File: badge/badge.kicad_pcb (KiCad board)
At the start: 2 copper layers, 39.4 x 73 mm, 13 parts, among them K1 KEYSW, K2 KEYSW, K3 KEYSW, K4 KEYSW, U1 ProMicro

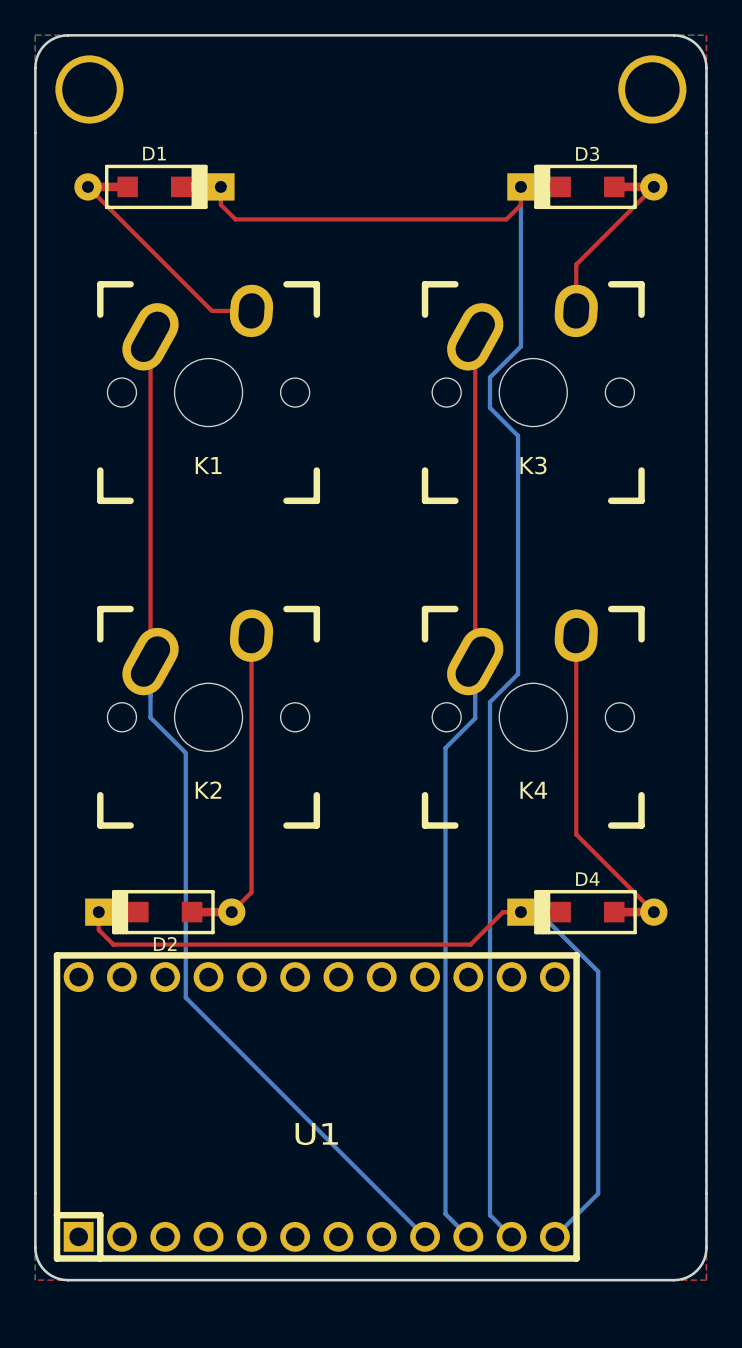
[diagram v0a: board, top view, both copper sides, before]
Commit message: Use different pro micro pins for easier routing
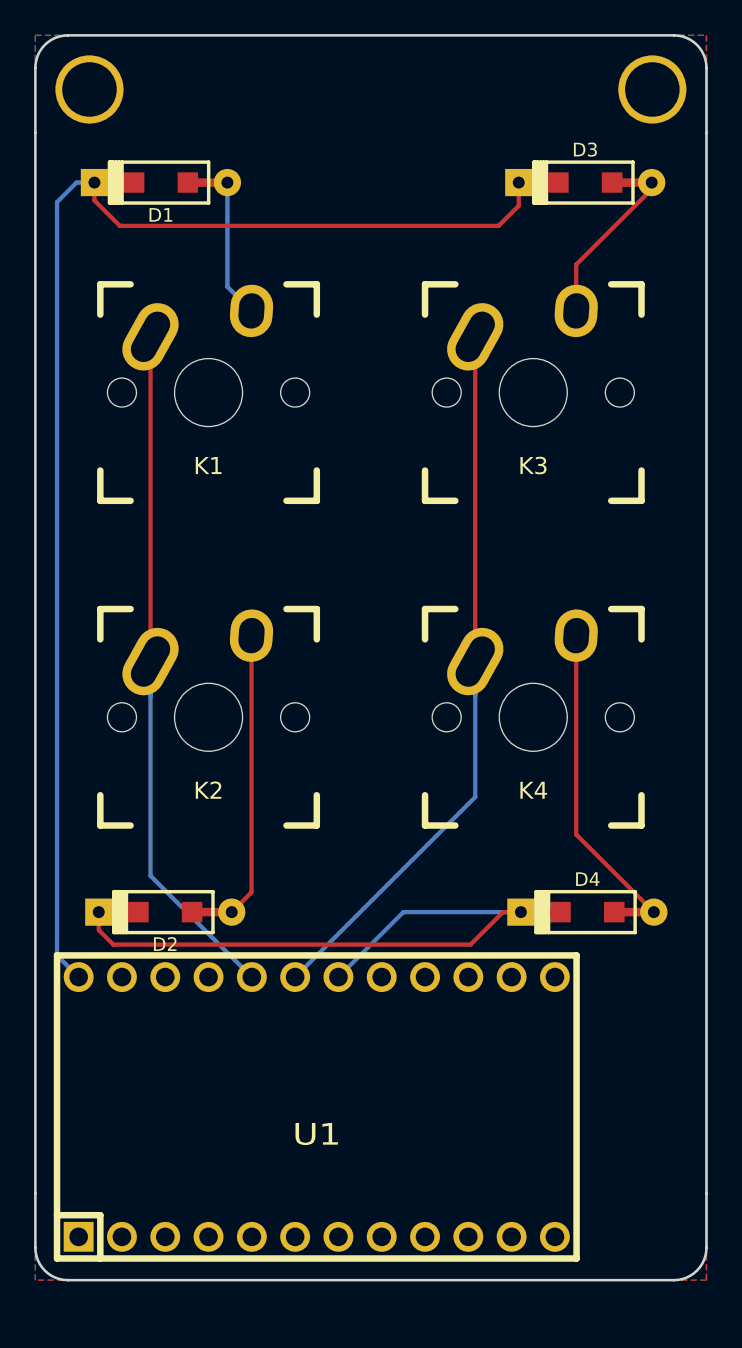
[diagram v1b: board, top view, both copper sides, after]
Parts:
- moved D1 0.46 mm to (117.9, 29.0), turned to 0 degrees
- moved D3 0.28 mm to (142.7, 29.0)
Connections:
- U1 pad 10: /col1 -> Net-(U1-Pad10)
- U1 pad 11: /row0 -> Net-(U1-Pad11)
- U1 pad 12: /row1 -> Net-(U1-Pad12)
- U1 pad 13: Net-(U1-Pad13) -> /row0
- U1 pad 17: Net-(U1-Pad17) -> /col0
- U1 pad 18: Net-(U1-Pad18) -> /col1
- U1 pad 19: Net-(U1-Pad19) -> /row1
- U1 pad 23: Net-(U1-Pad23) -> GND
- U1 pad 3: Net-(U1-Pad3) -> GND
- U1 pad 9: /col0 -> Net-(U1-Pad9)
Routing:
- net /col0: track 59.5 -> 42.0 mm
- net /row1: track 49.6 -> 39.2 mm
- net /col1: track 54.1 -> 43.9 mm
- net /row0: track 84.6 -> 77.1 mm
- net Net-(D1-Pad2): track 12.6 -> 8.11 mm

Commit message: Use SparkFun library, the keebs pro micro is wrong
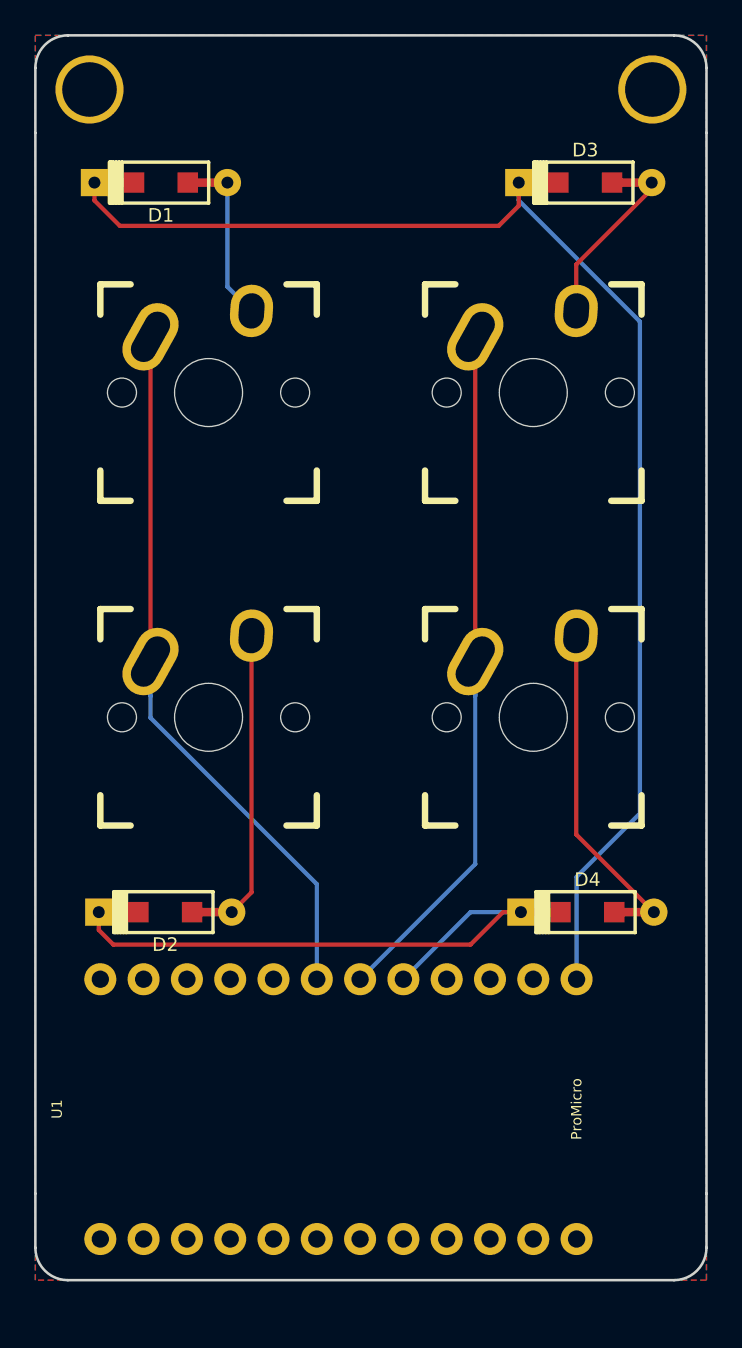
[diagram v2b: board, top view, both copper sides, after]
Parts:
- U1: footprint keebs:Pro_Micro -> sparkfun_boards:SPARKFUN_PRO_MICRO
- moved U1 0.13 mm to (127.0, 83.3), turned to 90 degrees
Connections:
- U1 pad 17: /col0 -> /row1
- U1 pad 19: /row1 -> /col0
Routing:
- net /row1: track 39.2 -> 35.5 mm
- net /row0: track 77.1 -> 79.6 mm
- net /col1: track 43.9 -> 42.5 mm
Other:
- board text added: "https://harding.coffee/2019/05/pdxkbc/"

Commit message: Update revision to v3.0
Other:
- board text added: "rev v3.0"
- board text removed: "rev v2.0"
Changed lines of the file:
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@@
     (effects (font (size 0.9 0.9) (thickness 0.2)) (justify mirror))
   )
-  (gr_text "rev v2.0" (at 147.955 88.9 270) (layer B.Mask)
+  (gr_text "rev v3.0" (at 147.955 88.9 270) (layer B.Mask)
     (effects (font (size 1 1) (thickness 0.2)) (justify mirror))
   )

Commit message: 2x3 layout and case
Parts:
- added D3: D, keyboard_parts:D_SOD123_axial, B.Cu at (118.7, 87.6)
- added D6: D, keyboard_parts:D_SOD123_axial, B.Cu at (141.0, 87.6)
- added HOLE_M3: VAL**, keyboard_parts:HOLE_M3, F.Cu at (146.1, 91.4)
- added HOLE_M3: VAL**, keyboard_parts:HOLE_M3, F.Cu at (114.3, 91.4)
- added K3: KEYSW, keebs:Mx_Alps_100, F.Cu at (120.7, 79.3)
- added K6: KEYSW, keebs:Mx_Alps_100, F.Cu at (139.6, 79.3)
- D1, D2, U1: moved to B.Cu
- D4: renamed from D3; moved to B.Cu
- D5: renamed from D4; moved to B.Cu
- G***: moved to F.Cu
- moved G*** 64.9 mm to (130.2, 90.2)
- moved U1 42.0 mm to (127.0, 41.3), turned to 270 degrees
- moved G*** 39.9 mm to (129.5, 69.8), turned to 0 degrees
- moved HOLE_M3 32.9 mm to (146.1, 29.2)
- moved HOLE_M3 32.9 mm to (114.3, 29.2)
- moved D4 23.2 mm to (141.0, 52.1)
- moved D1 23.1 mm to (118.7, 52.1)
- moved D5 3.70 mm to (141.0, 68.6)
- moved D2 3.24 mm to (118.7, 68.6)
- moved K4 0.11 mm to (139.6, 41.4)
- moved K1 0.08 mm to (120.7, 41.4)
- moved K5 0.08 mm to (139.6, 60.3)
- renumbered K3 to K4, K4 to K5
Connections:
- U1 pad 10: Net-(U1-Pad10) -> /col1
- U1 pad 13: /row0 -> /row1
- U1 pad 17: /row1 -> /row0
- U1 pad 18: /col1 -> Net-(U1-Pad18)
- U1 pad 19: /col0 -> Net-(U1-Pad19)
- U1 pad 20: Net-(U1-Pad20) -> /row2
- U1 pad 5: Net-(U1-Pad5) -> /col0
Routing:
- net /row2: track 0.00 -> 67.0 mm
- net /row0: track 79.6 -> 24.9 mm
- net Net-(D6-Pad2): track 0.00 -> 14.0 mm
- net Net-(D3-Pad2): track 0.00 -> 13.3 mm
- net /row1: track 35.5 -> 47.7 mm
- net /col0: track 41.7 -> 50.5 mm
- net Net-(D1-Pad2): track 8.11 -> 15.7 mm
- net Net-(D4-Pad2): track 9.16 -> 16.6 mm
- net /col1: track 42.5 -> 46.7 mm
- net Net-(D5-Pad2): track 18.1 -> 14.2 mm
- net Net-(D2-Pad2): track 16.7 -> 13.3 mm
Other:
- board size 39.4 x 73 mm -> 39.4 x 69.8 mm
- board text added: "Hack the Planet"
- board text added: "Keep Portland Weird"
- board text added: "https://pdxkbc.com/"
- board text added: "smooth side down"
- board text added: "usb"
